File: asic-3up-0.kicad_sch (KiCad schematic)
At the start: 65 parts, among them J12 Conn_01x01, J13 Conn_01x01, J18 Conn_01x01, J3 Conn_01x01, J4 Conn_01x01, U28 MCP1824T-1202E/OT, U29 MCP1824T-1202E/OT, U30 MCP1824T-1202E/OT, U32 MCP1824T-0802E, U42 MCP1824T-0802E, U43 MCP1824T-0802E, U45 BM1362AC_MODE1, U46 BM1362AC_MODE0, U47 BM1362AC_MODE1

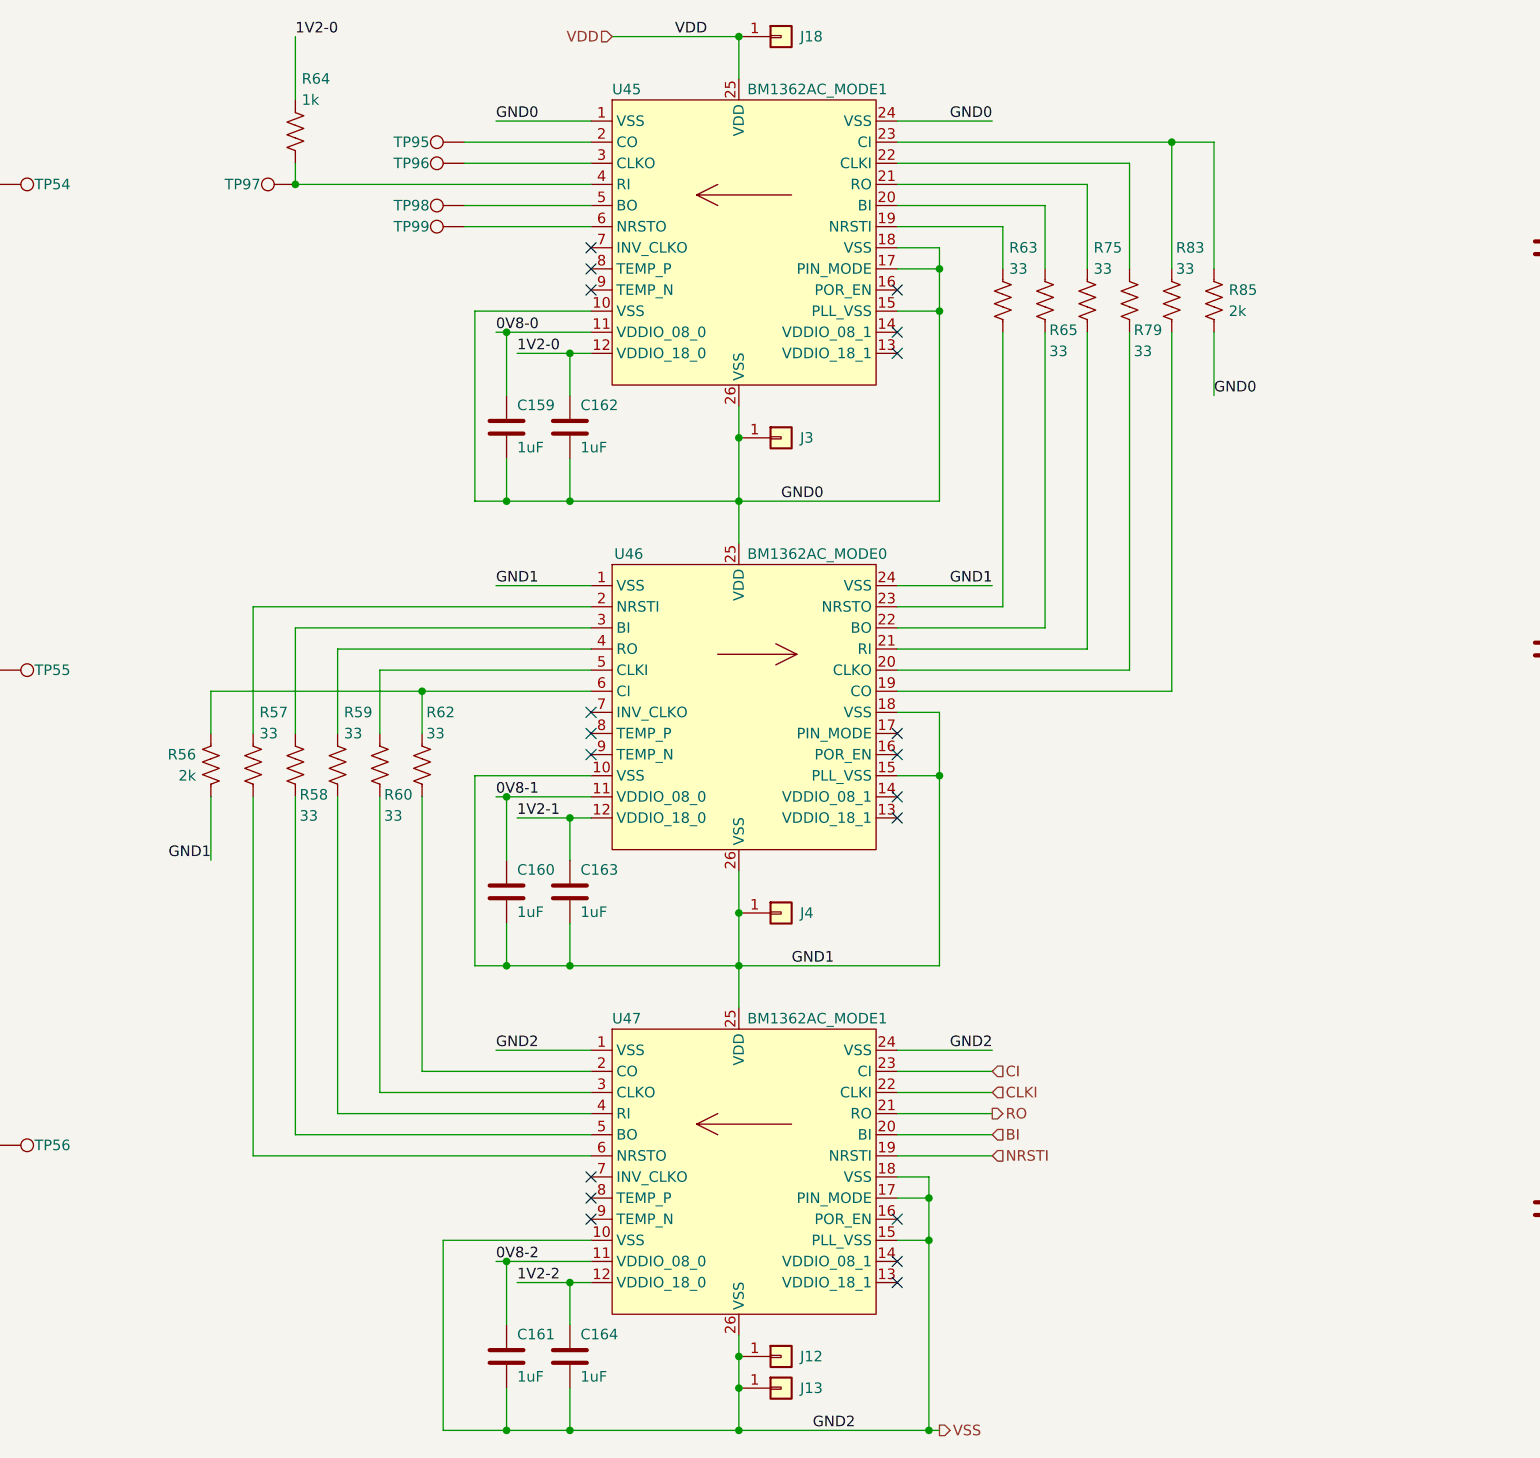
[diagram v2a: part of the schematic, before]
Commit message: added fix for #22. deleted old gerbers
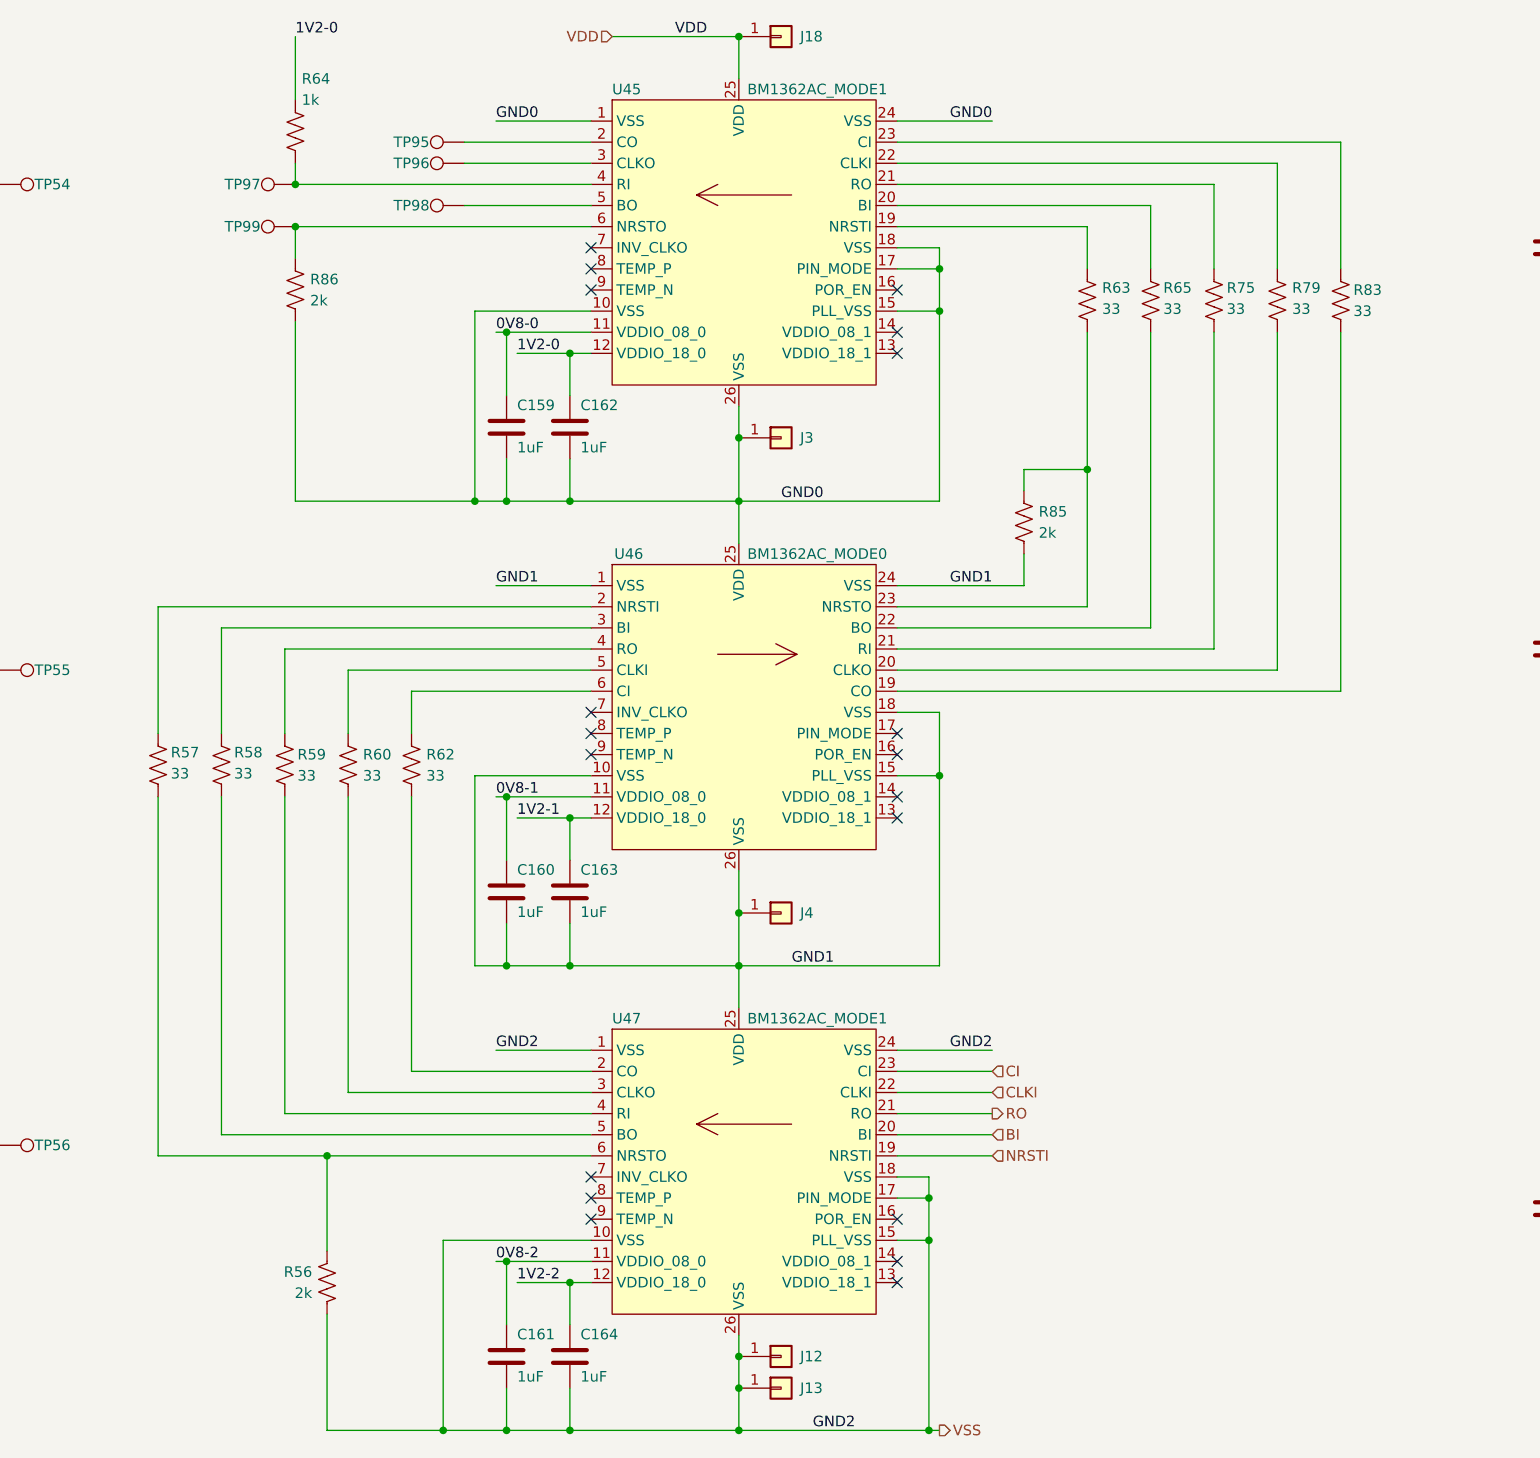
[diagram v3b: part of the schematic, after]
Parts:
- added R86: 2k, Resistor_SMD:R_0402_1005Metric, symbol Device:R_US
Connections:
- net GND0: now also R86.2; no longer R85.2
- net GND1: now also R85.2; no longer R56.2
- net VSS: now also R56.2
- net at R83.1, U45.23 (CI): no longer R85.1
- net at R62.1, U46.6 (CI): no longer R56.1
- net at TP99.1, U45.6 (NRSTO): now also R86.1
- net at R63.2, U46.23 (NRSTO): now also R85.1
- net at R57.2, U47.6 (NRSTO): now also R56.1
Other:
- moved on the sheet: R56, R57, R58, R59, R60, R62, R63, R65, R75, R79, R83, R85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

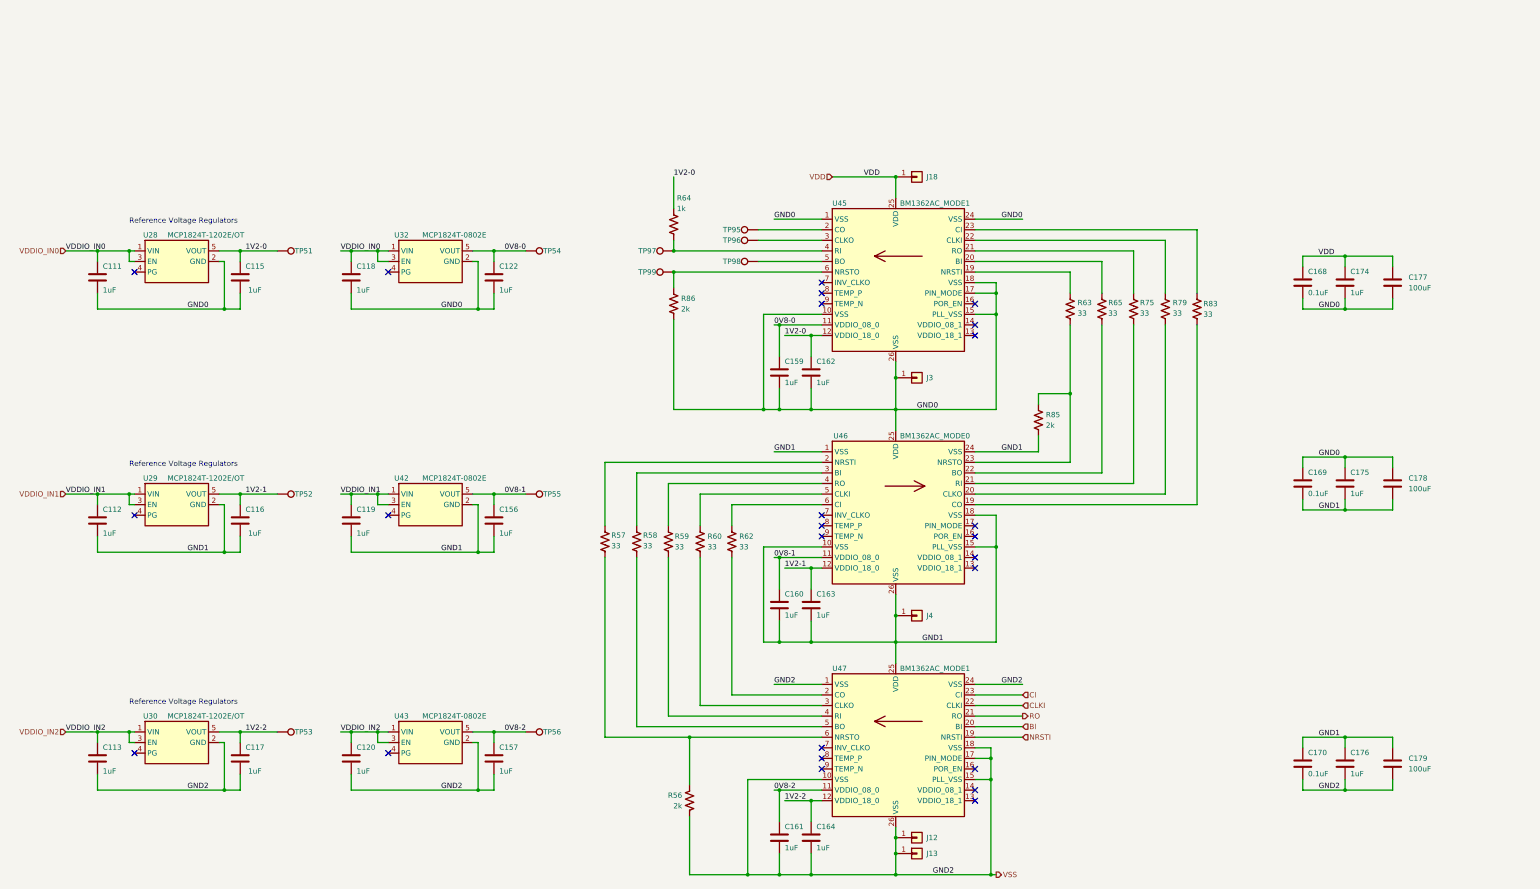
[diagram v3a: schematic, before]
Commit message: reduced center pad paste amount. cleaned up ASIC footprint vias. moved vreg passives around to better fit model name
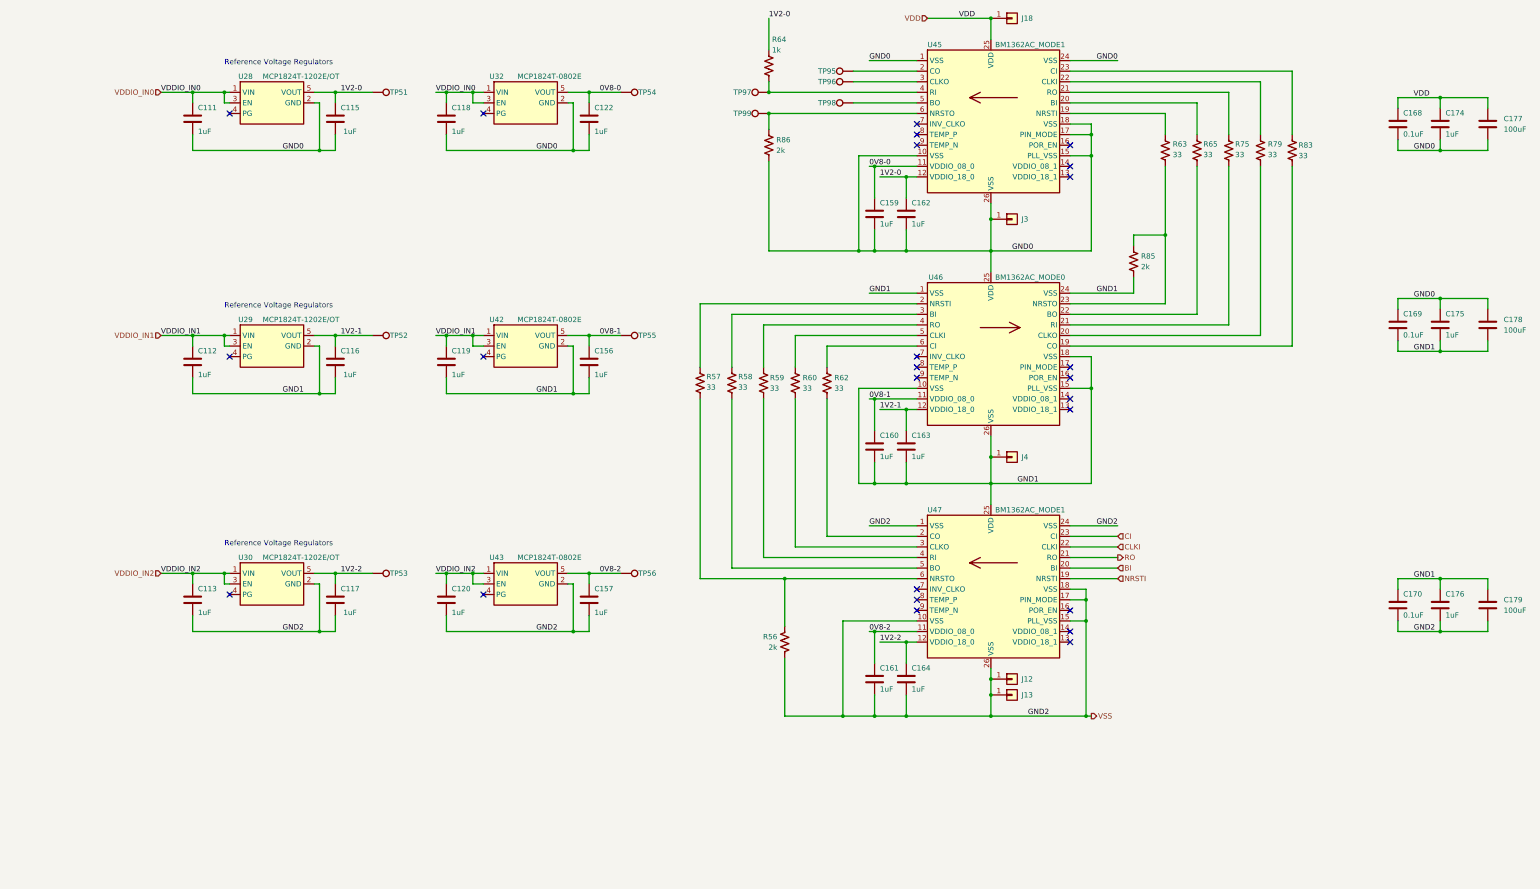
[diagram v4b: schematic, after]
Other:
- moved on the sheet: C111, C112, C113, C115, C116, C117, C118, C119, C120, C122, C156, C157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

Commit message: bumped version to v4. added USB protection diodes for #31. added power TVS diodes for #28. changed snubber resistors to higher wattage and located closer to mosfets for #27 and #30.
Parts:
- C168, C169, C170: DK 1276-1234-1-ND -> 478-KGM05AR71C104KHCT-ND; PARTNO CL05A104KO5NNNC -> KGM05AR71C104KH
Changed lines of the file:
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@@
 	(title_block
 		(title "emberOne/00")
-		(date "2025-02-25")
-		(rev "3")
+		(date "2025-04-21")
+		(rev "4")
 	)
 	(text "Reference Voltage Regulators"
@@
 			)
 		)
-		(property "DK" "1276-1234-1-ND"
+		(property "DK" "478-KGM05AR71C104KHCT-ND"
 			(at 346.71 80.01 0)
 			(effects
@@
 			)
 		)
-		(property "PARTNO" "CL05A104KO5NNNC"
+		(property "PARTNO" "KGM05AR71C104KH"
 			(at 346.71 80.01 0)
 			(effects
@@
 			)
 		)
-		(property "DK" "1276-1234-1-ND"
+		(property "DK" "478-KGM05AR71C104KHCT-ND"
 			(at 346.71 195.58 0)
 			(effects
@@
 			)
 		)
-		(property "PARTNO" "CL05A104KO5NNNC"
+		(property "PARTNO" "KGM05AR71C104KH"
 			(at 346.71 195.58 0)
 			(effects
@@
 			)
 		)
-		(property "DK" "1276-1234-1-ND"
+		(property "DK" "478-KGM05AR71C104KHCT-ND"
 			(at 346.71 128.27 0)
 			(effects
@@
 			)
 		)
-		(property "PARTNO" "CL05A104KO5NNNC"
+		(property "PARTNO" "KGM05AR71C104KH"
 			(at 346.71 128.27 0)
 			(effects

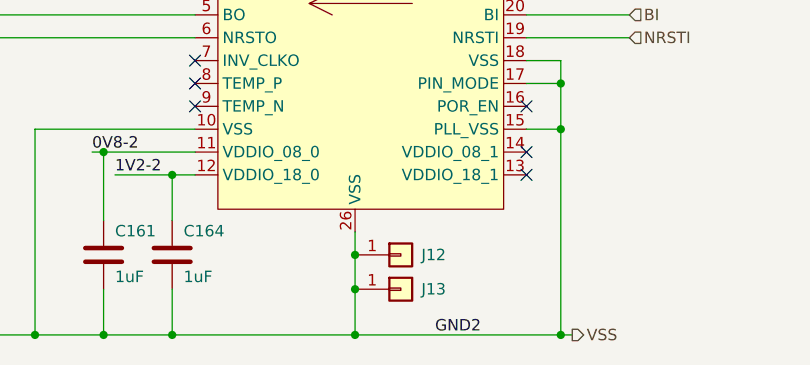
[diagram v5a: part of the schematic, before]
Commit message: move most components away from the edges of the PCB
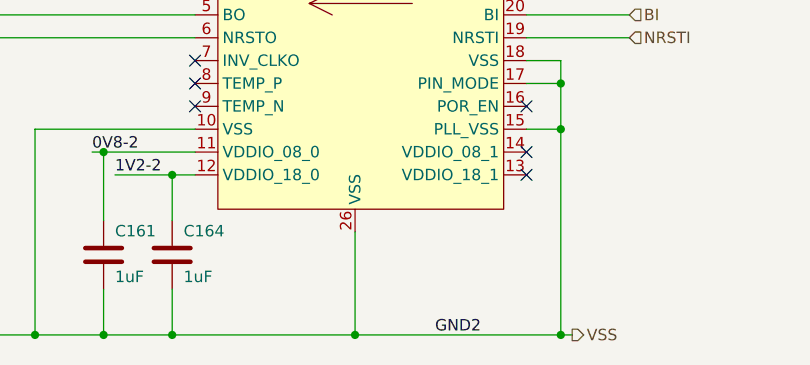
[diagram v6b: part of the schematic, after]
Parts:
- removed J12: Conn_01x01, emberone:14x9_powertab_L, symbol Connector_Generic:Conn_01x01
- removed J13: Conn_01x01, emberone:14x9_powertab_R, symbol Connector_Generic:Conn_01x01
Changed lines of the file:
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@@
 	)
 	(junction
-		(at 248.92 213.36)
-		(diameter 0)
-		(color 0 0 0 0)
-	)
-	(junction
 		(at 228.6 166.37)
 		(diameter 0)
@@
 	)
 	(junction
-		(at 248.92 217.17)
-		(diameter 0)
-		(color 0 0 0 0)
-	)
-	(junction
 		(at 248.92 102.87)
 		(diameter 0)
@@
 	(wire
 		(pts
-			(xy 248.92 213.36) (xy 248.92 217.17)
-		)
-		(stroke
-			(width 0)
-			(type default)
-		)
-	)
-	(wire
-		(pts
 			(xy 64.77 190.5) (xy 66.04 190.5)
 		)
@@
 	(wire
 		(pts
-			(xy 248.92 210.82) (xy 248.92 213.36)
+			(xy 248.92 210.82) (xy 248.92 222.25)
 		)
 		(stroke
@@
 	(wire
 		(pts
-			(xy 248.92 217.17) (xy 248.92 222.25)
-		)
-		(stroke
-			(width 0)
-			(type default)
-		)
-	)
-	(wire
-		(pts
 			(xy 115.57 130.81) (xy 118.11 130.81)
 		)
@@
 	)
 	(symbol
-		(lib_id "Connector_Generic:Conn_01x01")
-		(at 254 217.17 0)
-		(unit 1)
-		(exclude_from_sim no)
-		(in_bom yes)
-		(on_board yes)
-		(dnp no)
-		(property "Reference" "J13"
-			(at 256.286 217.17 0)
-			(effects
-				(font
-					(size 1.27 1.27)
-				)
-				(justify left)
-			)
-		)
-		(property "Value" "Conn_01x01"
-			(at 256.54 218.4399 0)
-			(effects
-				(font
-					(size 1.27 1.27)
-				)
-				(justify left)
-				(hide yes)
-			)
-		)
-		(property "Footprint" "emberone:14x9_powertab_R"
-			(at 254 217.17 0)
-			(effects
-				(font
-					(size 1.27 1.27)
-				)
-				(hide yes)
-			)
-		)
-		(property "Datasheet" "~"
-			(at 254 217.17 0)
-			(effects
-				(font
-					(size 1.27 1.27)
-				)
-				(hide yes)
-			)
-		)
-		(property "Description" "powertab"
-			(at 254 217.17 0)
-			(effects
-				(font
-					(size 1.27 1.27)
-				)
-				(hide yes)
-			)
-		)
-		(pin "1"
-		)
-		(instances
-			(project "emberone"
-				(path "/b036224c-4cdf-48cc-81df-19bc5283ebd2/dea5684e-9ec9-4967-b9ef-d4ee852a3fa0"
-					(reference "J13")
-					(unit 1)
-				)
-			)
-		)
-	)
-	(symbol
 		(lib_id "Device:C")
 		(at 118.11 78.74 0)
@@
 					(unit 1)
 				)
-			)
-		)
-	)
-	(symbol
-		(lib_id "Connector_Generic:Conn_01x01")
-		(at 254 213.36 0)
-		(unit 1)
-		(exclude_from_sim no)
-		(in_bom yes)
-		(on_board yes)
-		(dnp no)
-		(property "Reference" "J12"
-			(at 256.286 213.36 0)
-			(effects
-				(font
-					(size 1.27 1.27)
-				)
-				(justify left)
-			)
-		)
-		(property "Value" "Conn_01x01"
-			(at 256.54 214.6299 0)
-			(effects
-				(font
-					(size 1.27 1.27)
-				)
-				(justify left)
-				(hide yes)
-			)
-		)
-		(property "Footprint" "emberone:14x9_powertab_L"
-			(at 254 213.36 0)
-			(effects
-				(font
-					(size 1.27 1.27)
-				)
-				(hide yes)
-			)
-		)
-		(property "Datasheet" "~"
-			(at 254 213.36 0)
-			(effects
-				(font
-					(size 1.27 1.27)
-				)
-				(hide yes)
-			)
-		)
-		(property "Description" "powertab"
-			(at 254 213.36 0)
-			(effects
-				(font
-					(size 1.27 1.27)
-				)
-				(hide yes)
-			)
-		)
-		(pin "1"
-		)
-		(instances
-			(project "emberone"
-				(path "/b036224c-4cdf-48cc-81df-19bc5283ebd2/dea5684e-9ec9-4967-b9ef-d4ee852a3fa0"
-					(reference "J12")
-					(unit 1)
-				)

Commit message: added LDO alt part numbers
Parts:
- U28, U29, U30: ALT1 (none) -> LDK120M12R
- U32, U42, U43: ALT1 (none) -> LDK120M08R
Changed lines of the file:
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@@
 			)
 		)
+		(property "ALT1" "LDK120M08R"
+			(at 137.16 189.23 0)
+			(effects
+				(font
+					(size 1.27 1.27)
+				)
+				(hide yes)
+			)
+		)
 		(pin "1"
 		)
@@
 			)
 		)
+		(property "ALT1" "LDK120M08R"
+			(at 137.16 132.08 0)
+			(effects
+				(font
+					(size 1.27 1.27)
+				)
+				(hide yes)
+			)
+		)
 		(pin "1"
 		)
@@
 			)
 		)
+		(property "ALT1" "LDK120M12R"
+			(at 76.2 73.66 0)
+			(effects
+				(font
+					(size 1.27 1.27)
+				)
+				(hide yes)
+			)
+		)
 		(pin "1"
 		)
@@
 			)
 		)
+		(property "ALT1" "LDK120M12R"
+			(at 76.2 189.23 0)
+			(effects
+				(font
+					(size 1.27 1.27)
+				)
+				(hide yes)
+			)
+		)
 		(pin "1"
 		)
@@
 			)
 		)
+		(property "ALT1" "LDK120M12R"
+			(at 76.2 132.08 0)
+			(effects
+				(font
+					(size 1.27 1.27)
+				)
+				(hide yes)
+			)
+		)
 		(pin "1"
 		)
@@
 			(at 137.16 73.66 0)
 			(effects
+				(font
+					(size 1.27 1.27)
+				)
+				(hide yes)
+			)
+		)
+		(property "ALT1" "LDK120M08R"
+			(at 137.16 73.66 0)
+			(effects
